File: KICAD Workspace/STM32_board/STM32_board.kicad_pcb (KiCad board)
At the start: 2 copper layers, 171.4 x 138.7 mm, 27 parts, among them J1 Power connector, J10 Low side connector, J11 Output pins, J2 High side connector, J3 Sensors connector, J4 LCD interface, J5 Low side connector, J6 3v3_out, J7 Joystick connector, J8 Output pins, J9 UART module, U1 CD4050BE, U2 LM7805_TO220, U3 LP2950-3.3_TO92

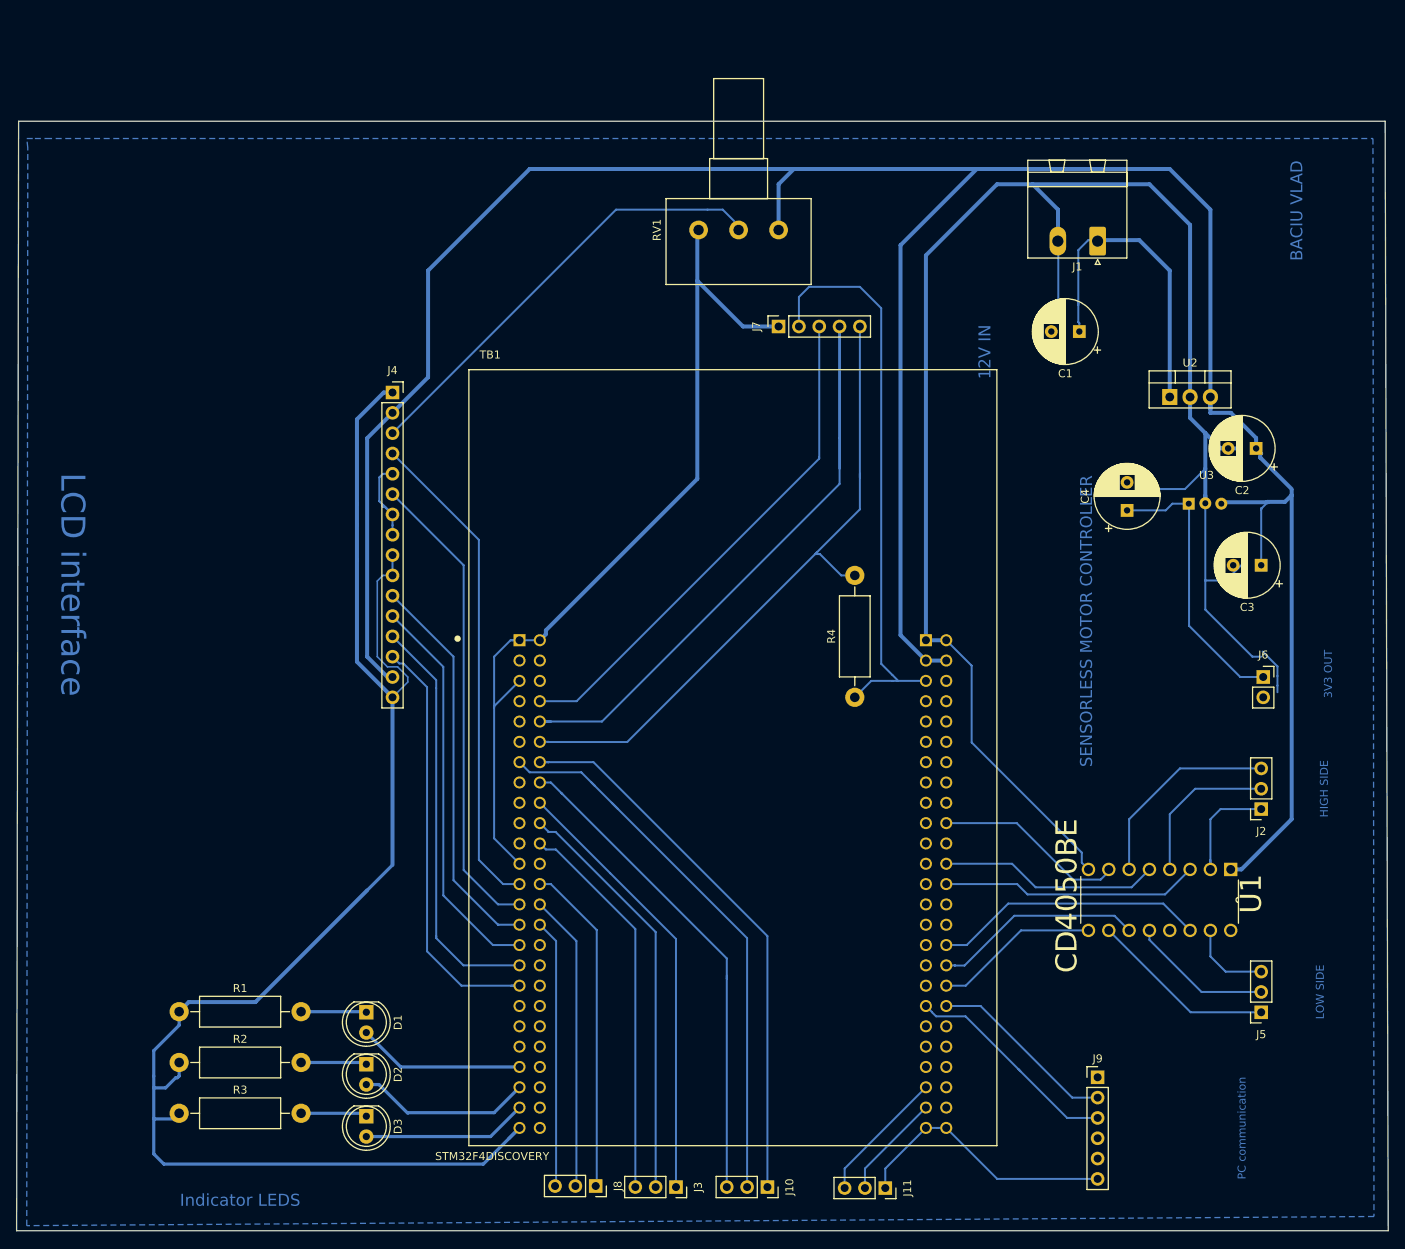
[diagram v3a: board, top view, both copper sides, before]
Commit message: SMD version
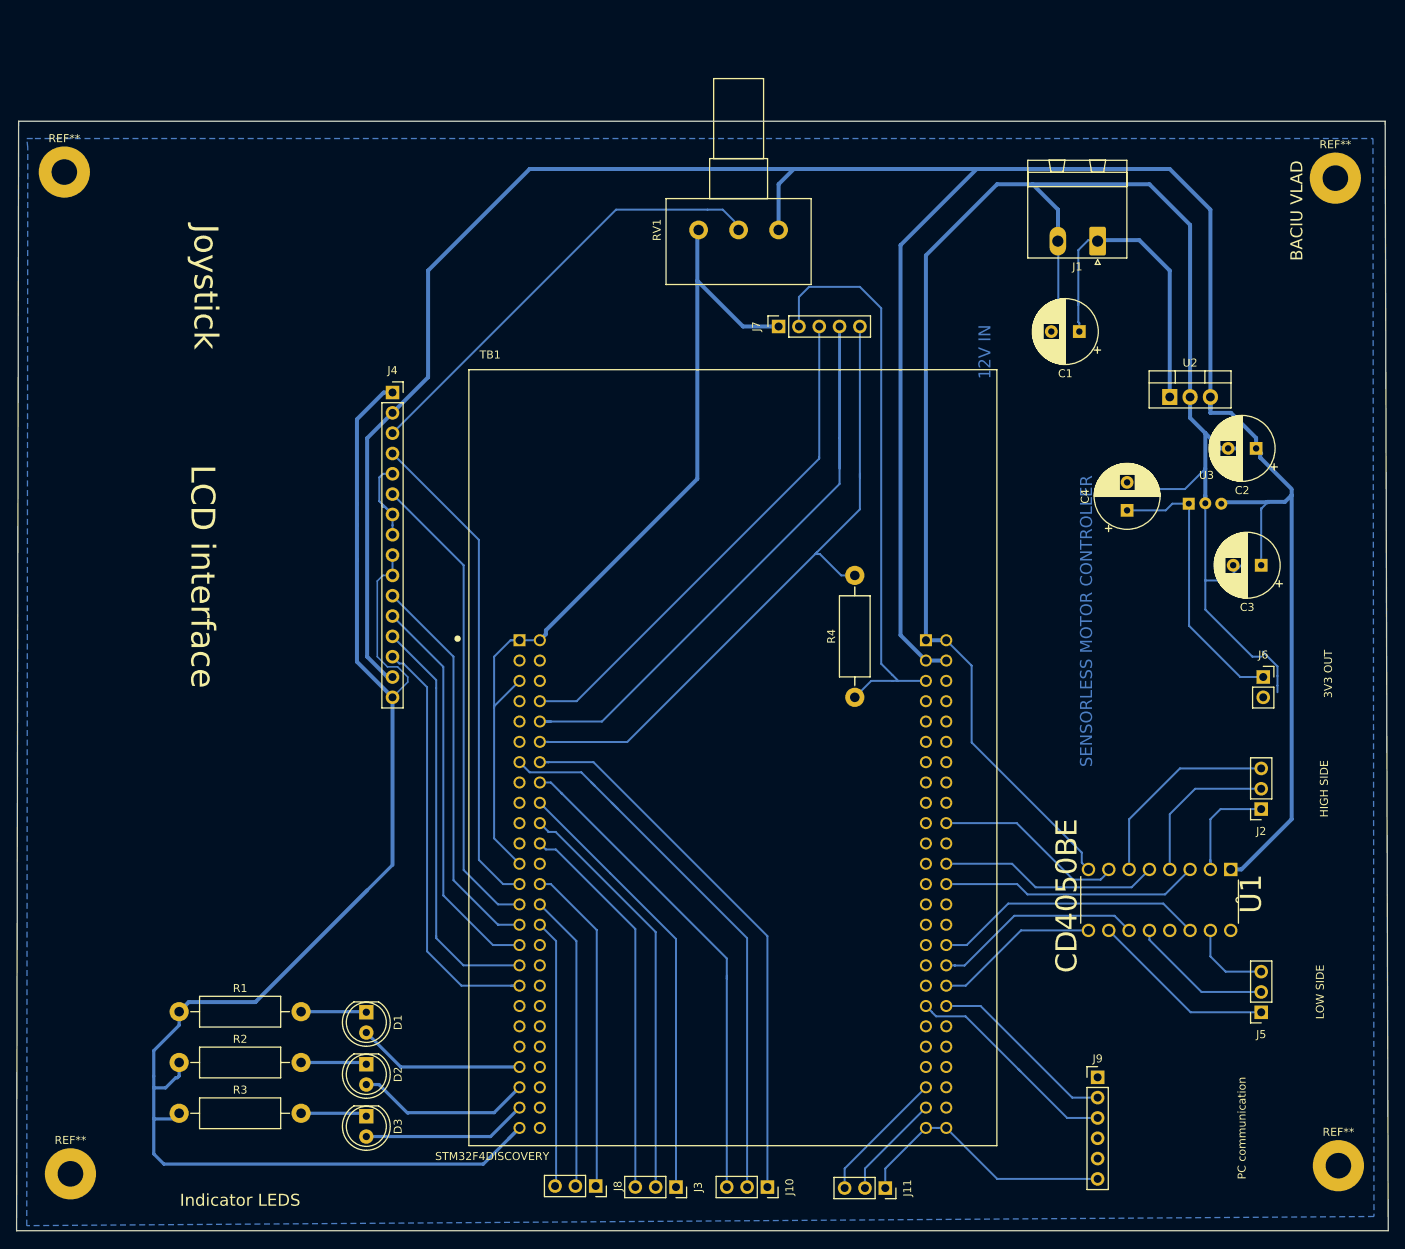
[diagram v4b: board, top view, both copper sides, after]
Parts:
- added REF**: MountingHole_3.2mm_M3_Pad, MountingHole:MountingHole_3.2mm_M3_Pad, F.Cu at (23.4, 33.4)
- added REF**: MountingHole_3.2mm_M3_Pad, MountingHole:MountingHole_3.2mm_M3_Pad, F.Cu at (24.1, 158.6)
- added REF**: MountingHole_3.2mm_M3_Pad, MountingHole:MountingHole_3.2mm_M3_Pad, F.Cu at (182.6, 157.6)
- added REF**: MountingHole_3.2mm_M3_Pad, MountingHole:MountingHole_3.2mm_M3_Pad, F.Cu at (182.2, 34.2)
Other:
- board text added: "Joystick"
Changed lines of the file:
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@@
   (general
     (thickness 1.6)
-    (drawings 14)
+    (drawings 15)
     (tracks 354)
     (zones 0)
-    (modules 27)
+    (modules 31)
     (nets 104)
   )
@@
     (35 F.Paste user)
     (36 B.SilkS user)
-    (37 F.SilkS user hide)
+    (37 F.SilkS user)
     (38 B.Mask user)
     (39 F.Mask user)
@@
     (mod_text_size 1 1)
     (mod_text_width 0.15)
-    (pad_size 9 9)
-    (pad_drill 6)
+    (pad_size 6.4 6.4)
+    (pad_drill 3.2)
     (pad_to_mask_clearance 0.051)
     (solder_mask_min_width 0.25)
@@
       (drillshape 0)
       (scaleselection 1)
-      (outputdirectory "../../../../Users/vlad.baciu/Desktop/"))
+      (outputdirectory "Output files/"))
   )
   (net 0 "")
@@
     )
   )
+  (module MountingHole:MountingHole_3.2mm_M3_Pad (layer F.Cu)
+    (at 23.368 33.401)
+    (descr "Mounting Hole 3.2mm, M3")
+    (tags "mounting hole 3.2mm m3")
+    (attr virtual)
+    (fp_text reference REF** (at 0 -4.2) (layer F.SilkS)
+      (effects (font (size 1 1) (thickness 0.15)))
+    )
+    (fp_text value MountingHole_3.2mm_M3_Pad (at 0 4.2) (layer F.Fab)
+      (effects (font (size 1 1) (thickness 0.15)))
+    )
+    (fp_circle (center 0 0) (end 3.45 0) (layer F.CrtYd) (width 0.05))
+    (fp_circle (center 0 0) (end 3.2 0) (layer Cmts.User) (width 0.15))
+    (fp_text user %R (at 0.3 0) (layer F.Fab)
+      (effects (font (size 1 1) (thickness 0.15)))
+    )
+    (pad 1 thru_hole circle (at 0 0) (size 6.4 6.4) (drill 3.2) (layers *.Cu *.Mask))
+  )
+  (module MountingHole:MountingHole_3.2mm_M3_Pad (layer F.Cu)
+    (at 24.13 158.623)
+    (descr "Mounting Hole 3.2mm, M3")
+    (tags "mounting hole 3.2mm m3")
+    (attr virtual)
+    (fp_text reference REF** (at 0 -4.2) (layer F.SilkS)
+      (effects (font (size 1 1) (thickness 0.15)))
+    )
+    (fp_text value MountingHole_3.2mm_M3_Pad (at 0 4.2) (layer F.Fab)
+      (effects (font (size 1 1) (thickness 0.15)))
+    )
+    (fp_circle (center 0 0) (end 3.45 0) (layer F.CrtYd) (width 0.05))
+    (fp_circle (center 0 0) (end 3.2 0) (layer Cmts.User) (width 0.15))
+    (fp_text user %R (at 0.3 0) (layer F.Fab)
+      (effects (font (size 1 1) (thickness 0.15)))
+    )
+    (pad 2 thru_hole circle (at 0 0) (size 6.4 6.4) (drill 3.2) (layers *.Cu *.Mask))
+  )
+  (module MountingHole:MountingHole_3.2mm_M3_Pad (layer F.Cu)
+    (at 182.626 157.607)
+    (descr "Mounting Hole 3.2mm, M3")
+    (tags "mounting hole 3.2mm m3")
+    (attr virtual)
+    (fp_text reference REF** (at 0 -4.2) (layer F.SilkS)
+      (effects (font (size 1 1) (thickness 0.15)))
+    )
+    (fp_text value MountingHole_3.2mm_M3_Pad (at 0 4.2) (layer F.Fab)
+      (effects (font (size 1 1) (thickness 0.15)))
+    )
+    (fp_circle (center 0 0) (end 3.45 0) (layer F.CrtYd) (width 0.05))
+    (fp_circle (center 0 0) (end 3.2 0) (layer Cmts.User) (width 0.15))
+    (fp_text user %R (at 0.3 0) (layer F.Fab)
+      (effects (font (size 1 1) (thickness 0.15)))
+    )
+    (pad 3 thru_hole circle (at 0 0) (size 6.4 6.4) (drill 3.2) (layers *.Cu *.Mask))
+  )
+  (module MountingHole:MountingHole_3.2mm_M3_Pad (layer F.Cu)
+    (at 182.245 34.163)
+    (descr "Mounting Hole 3.2mm, M3")
+    (tags "mounting hole 3.2mm m3")
+    (attr virtual)
+    (fp_text reference REF** (at 0 -4.2) (layer F.SilkS)
+      (effects (font (size 1 1) (thickness 0.15)))
+    )
+    (fp_text value MountingHole_3.2mm_M3_Pad (at 0 4.2) (layer F.Fab)
+      (effects (font (size 1 1) (thickness 0.15)))
+    )
+    (fp_circle (center 0 0) (end 3.45 0) (layer F.CrtYd) (width 0.05))
+    (fp_circle (center 0 0) (end 3.2 0) (layer Cmts.User) (width 0.15))
+    (fp_text user %R (at 0.3 0) (layer F.Fab)
+      (effects (font (size 1 1) (thickness 0.15)))
+    )
+    (pad 4 thru_hole circle (at 0 0) (size 6.4 6.4) (drill 3.2) (layers *.Cu *.Mask))
+  )
+  (gr_text "Joystick\n" (at 41.021 47.752 270) (layer F.SilkS)
+    (effects (font (size 3 3) (thickness 0.375)))
+  )
+  (gr_text "BACIU VLAD" (at 177.419 38.227 90) (layer F.SilkS)
+    (effects (font (size 1.5 1.5) (thickness 0.3)))
+  )
+  (gr_text "PC communication" (at 170.561 152.908 90) (layer F.SilkS)
+    (effects (font (size 1 1) (thickness 0.25)))
+  )
+  (gr_text "LOW SIDE" (at 180.34 135.89 90) (layer F.SilkS)
+    (effects (font (size 1 1) (thickness 0.25)))
+  )
   (gr_text "12V IN" (at 138.43 55.88 90) (layer B.Cu)
     (effects (font (size 1.5 1.5) (thickness 0.3)))
@@
   (gr_line (start 188.468 27.051) (end 188.468 27.051) (layer Edge.Cuts) (width 0.15))
   (gr_line (start 188.849 165.735) (end 188.468 27.051) (layer Edge.Cuts) (width 0.15))
-  (gr_text "PC communication" (at 170.561 152.908 90) (layer B.Cu)
-    (effects (font (size 1 1) (thickness 0.25)))
-  )
-  (gr_text "BACIU VLAD" (at 177.419 38.227 90) (layer B.Cu)
-    (effects (font (size 1.5 1.5) (thickness 0.3)))
-  )
   (gr_text "SENSORLESS MOTOR CONTROLLER" (at 151.13 89.535 90) (layer B.Cu)
     (effects (font (size 1.5 1.5) (thickness 0.3)))
   )
-  (gr_text "Indicator LEDS" (at 45.339 161.925) (layer B.Cu)
+  (gr_text "Indicator LEDS" (at 45.339 161.925) (layer F.SilkS)
     (effects (font (size 1.5 1.5) (thickness 0.3)))
   )
-  (gr_text "LOW SIDE" (at 180.34 135.89 90) (layer B.Cu)
+  (gr_text "HIGH SIDE " (at 180.848 110.49 90) (layer F.SilkS)
     (effects (font (size 1 1) (thickness 0.25)))
   )
-  (gr_text "HIGH SIDE " (at 180.848 110.49 90) (layer B.Cu)
+  (gr_text "3V3 OUT" (at 181.356 96.139 90) (layer F.SilkS)
     (effects (font (size 1 1) (thickness 0.25)))
   )
-  (gr_text "3V3 OUT" (at 181.356 96.139 90) (layer B.Cu)
-    (effects (font (size 1 1) (thickness 0.25)))
-  )
-  (gr_text "LCD interface" (at 24.384 84.963 270) (layer B.Cu)
+  (gr_text "LCD interface" (at 40.64 83.947 270) (layer F.SilkS)
     (effects (font (size 3 3) (thickness 0.375)))
   )
@@
   (segment (start 123.444 157.965) (end 131.064 150.345) (width 0.25) (layer B.Cu) (net 88))
   (segment (start 123.444 160.655) (end 123.444 157.965) (width 0.25) (layer B.Cu) (net 88))
-  (segment (start 83.193408 120.015) (end 82.804 120.015) (width 0.25) (layer B.Cu) (net 103))
-  (segment (start 83.193408 120.254408) (end 82.804 119.865) (width 0.25) (layer B.Cu) (net 103))
   (segment (start 89.916 128.143) (end 89.916 160.02) (width 0.25) (layer B.Cu) (net 89))
   (segment (start 82.804 122.405) (end 84.178 122.405) (width 0.25) (layer B.Cu) (net 89))
@@
   (segment (start 120.904 157.965) (end 131.064 147.805) (width 0.25) (layer B.Cu) (net 102))
   (segment (start 120.904 160.655) (end 120.904 157.965) (width 0.25) (layer B.Cu) (net 102))
-  (zone (net 0) (net_name "") (layer B.Cu) (hatch edge 0.508)
-    (connect_pads (clearance 0.508))
-    (min_thickness 0.254)
-    (keepout (tracks not_allowed) (vias not_allowed) (copperpour not_allowed))
-    (fill (arc_segments 16) (thermal_gap 0.508) (thermal_bridge_width 0.508))
-    (polygon
-      (pts
-        (xy 19.431 67.564) (xy 30.226 67.818) (xy 30.353 101.346) (xy 20.066 101.219)
-      )
-    )
-  )
+  (segment (start 83.193408 120.015) (end 82.804 120.015) (width 0.25) (layer B.Cu) (net 103))
+  (segment (start 83.193408 120.254408) (end 82.804 119.865) (width 0.25) (layer B.Cu) (net 103))
   (zone (net 0) (net_name "") (layer B.Cu) (hatch edge 0.508)
     (connect_pads (clearance 0.8))
